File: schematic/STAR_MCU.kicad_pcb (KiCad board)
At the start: 2 copper layers, 168 parts, among them J11 6120XX21621_61200621621, J13 6120XX21621_61200821621, J14 6120XX21621_61200821621, J15 6120XX21621_61200821621, J16 6120XX21621_61200821621, J17 SSW-106-02-G-S-RA, J18 6120XX21621_61200621621, J19 6120XX21621_61200821621, J2 USB4216-03-A, J20 S5B-XH-A, J21 6120XX21621_61200621621, J22 SSW-106-02-G-S-RA, J23 Conn_02x20_Odd_Even, J24 HC-SR04, J25 HC-SR04, J26 HC-SR04, J27 HC-SR04, J28 Conn_01x02, J31 SSW-106-02-G-S-RA, J32 SSW-106-02-G-S-RA, J4 E1E2-Emulator-Interface, J5 SSW-106-02-G-S-RA, J6 SSW-106-02-G-D-RA, J7 USB4216-03-A, J8 Conn_02x20_Odd_Even, U1 R5F572NNHGFP-30, U2 CY7C65213A-28PVXI, U3 TVS2200DRV, U4 LDL1117S33R, U5 TPS2116DRLR, U6 TVS2200DRV, U7 DS18B20+

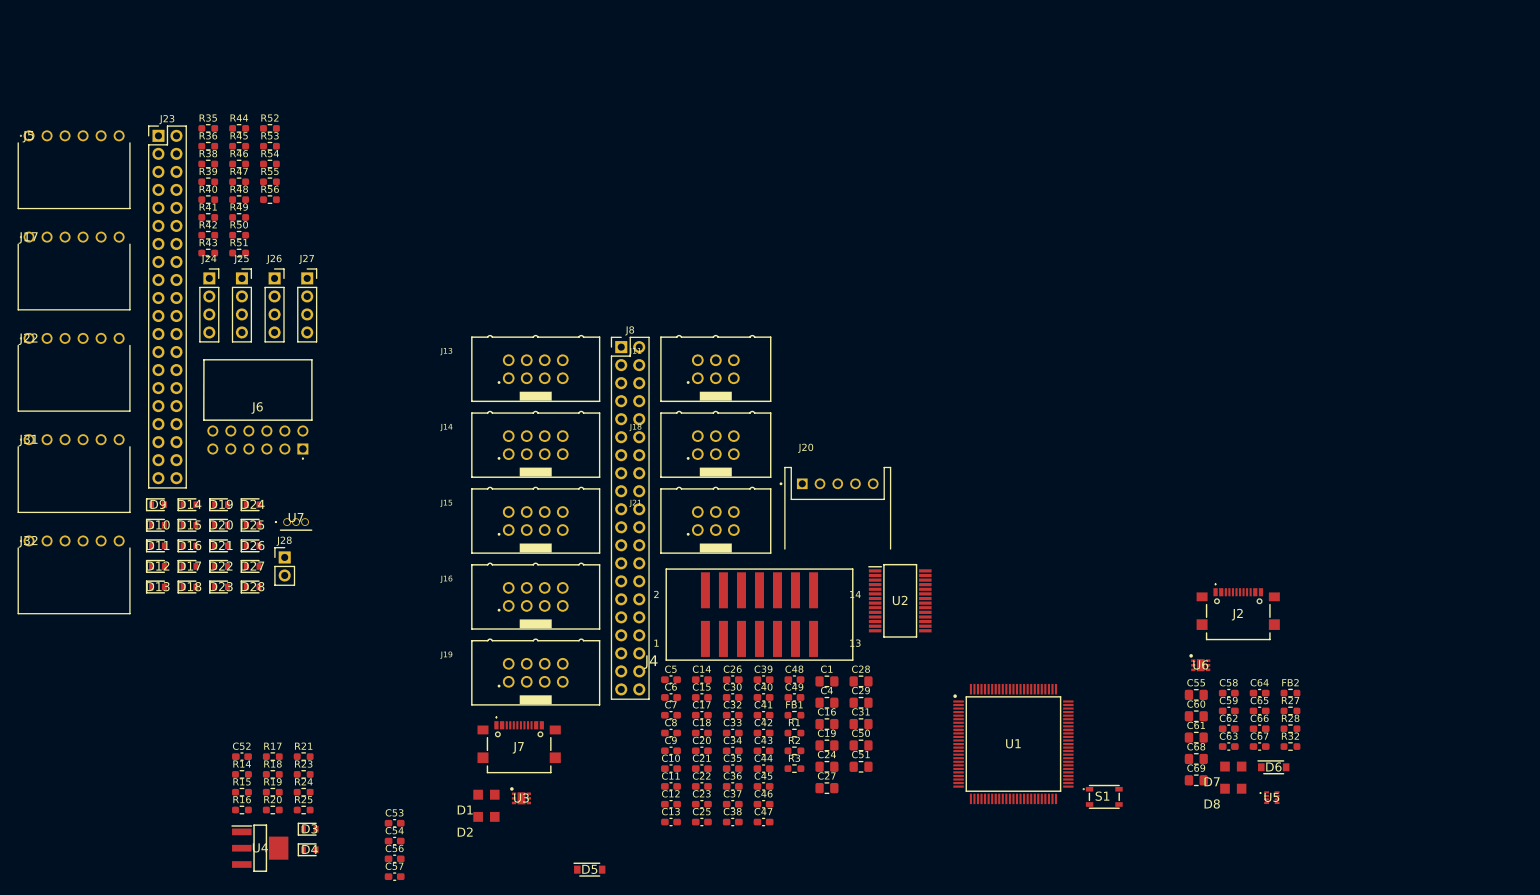
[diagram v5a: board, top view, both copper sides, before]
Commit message: docs(schematic): update KiCad file headers
Standardize schematic file metadata:
- Update date to 2026-01-01
- Update copyright to STAR Project
- Ensure consistency with firmware file headers
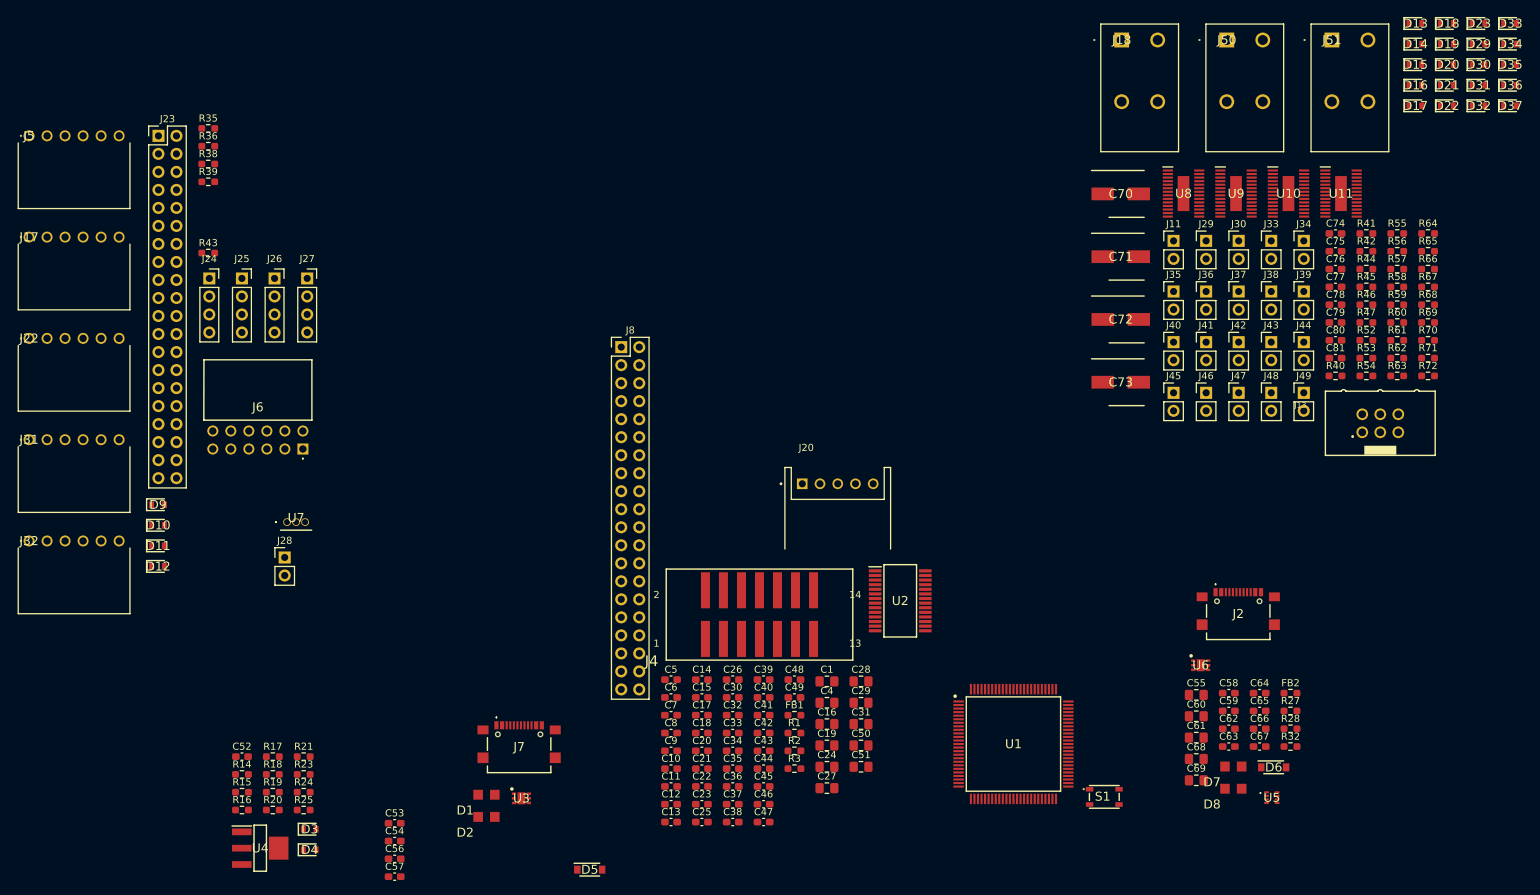
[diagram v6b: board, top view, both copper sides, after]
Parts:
- removed D24, D25, D26, D27, D28: RED, SML-D12Y1WT86:LEDC1608X55N
- removed J14, J15, J16, J19: 6120XX21621_61200821621, 61200821621:61200821621
- removed J21: 6120XX21621_61200621621, 61200621621:61200621621
- removed R48, R49, R50, R51: 68R, Resistor_SMD:R_0603_1608Metric_Pad0.98x0.95mm_HandSolder
- added C70: 56u, 865080343007:CAPAE660X550N, F.Cu at (197.9, 46.3)
- added C71: 56u, 865080343007:CAPAE660X550N, F.Cu at (197.9, 55.2)
- added C72: 56u, 865080343007:CAPAE660X550N, F.Cu at (197.9, 64.0)
- added C73: 56u, 865080343007:CAPAE660X550N, F.Cu at (197.9, 72.9)
- added C74: 220n, Capacitor_SMD:C_0603_1608Metric_Pad1.08x0.95mm_HandSolder, F.Cu at (228.1, 51.9)
- added C75: 220n, Capacitor_SMD:C_0603_1608Metric_Pad1.08x0.95mm_HandSolder, F.Cu at (228.1, 54.4)
- added C76: 220n, Capacitor_SMD:C_0603_1608Metric_Pad1.08x0.95mm_HandSolder, F.Cu at (228.1, 56.9)
- added C77: 220n, Capacitor_SMD:C_0603_1608Metric_Pad1.08x0.95mm_HandSolder, F.Cu at (228.1, 59.5)
- added C78: 100n, Capacitor_SMD:C_0603_1608Metric_Pad1.08x0.95mm_HandSolder, F.Cu at (228.1, 62.0)
- added C79: 100n, Capacitor_SMD:C_0603_1608Metric_Pad1.08x0.95mm_HandSolder, F.Cu at (228.1, 64.5)
- added C80: 100n, Capacitor_SMD:C_0603_1608Metric_Pad1.08x0.95mm_HandSolder, F.Cu at (228.1, 67.0)
- added C81: 100n, Capacitor_SMD:C_0603_1608Metric_Pad1.08x0.95mm_HandSolder, F.Cu at (228.1, 69.5)
- added D29: RED, SML-D12Y1WT86:LEDC1608X55N, F.Cu at (248.3, 25.2)
- added D30: RED, SML-D12Y1WT86:LEDC1608X55N, F.Cu at (248.3, 28.1)
- added D31: RED, SML-D12Y1WT86:LEDC1608X55N, F.Cu at (248.3, 31.0)
- added D32: RED, SML-D12Y1WT86:LEDC1608X55N, F.Cu at (248.3, 33.9)
- added D33: RED, SML-D12Y1WT86:LEDC1608X55N, F.Cu at (252.8, 22.3)
- added D34: RED, SML-D12Y1WT86:LEDC1608X55N, F.Cu at (252.8, 25.2)
- added D35: RED, SML-D12Y1WT86:LEDC1608X55N, F.Cu at (252.8, 28.1)
- added D36: RED, SML-D12Y1WT86:LEDC1608X55N, F.Cu at (252.8, 31.0)
- added D37: RED, SML-D12Y1WT86:LEDC1608X55N, F.Cu at (252.8, 33.9)
- added J29: Conn_01x02, Connector_PinHeader_2.54mm:PinHeader_1x02_P2.54mm_Vertical, F.Cu at (209.9, 53.0)
- added J30: Conn_01x02, Connector_PinHeader_2.54mm:PinHeader_1x02_P2.54mm_Vertical, F.Cu at (214.5, 53.0)
- added J33: Conn_01x02, Connector_PinHeader_2.54mm:PinHeader_1x02_P2.54mm_Vertical, F.Cu at (219.1, 53.0)
- added J34: Conn_01x02, Connector_PinHeader_2.54mm:PinHeader_1x02_P2.54mm_Vertical, F.Cu at (223.7, 53.0)
- added J35: Conn_01x02, Connector_PinHeader_2.54mm:PinHeader_1x02_P2.54mm_Vertical, F.Cu at (205.3, 60.1)
- added J36: Conn_01x02, Connector_PinHeader_2.54mm:PinHeader_1x02_P2.54mm_Vertical, F.Cu at (209.9, 60.1)
- added J37: Conn_01x02, Connector_PinHeader_2.54mm:PinHeader_1x02_P2.54mm_Vertical, F.Cu at (214.5, 60.1)
- added J38: Conn_01x02, Connector_PinHeader_2.54mm:PinHeader_1x02_P2.54mm_Vertical, F.Cu at (219.1, 60.1)
- added J39: Conn_01x02, Connector_PinHeader_2.54mm:PinHeader_1x02_P2.54mm_Vertical, F.Cu at (223.7, 60.1)
- added J40: Conn_01x02, Connector_PinHeader_2.54mm:PinHeader_1x02_P2.54mm_Vertical, F.Cu at (205.3, 67.2)
- added J41: Conn_01x02, Connector_PinHeader_2.54mm:PinHeader_1x02_P2.54mm_Vertical, F.Cu at (209.9, 67.2)
- added J42: Conn_01x02, Connector_PinHeader_2.54mm:PinHeader_1x02_P2.54mm_Vertical, F.Cu at (214.5, 67.2)
- added J43: Conn_01x02, Connector_PinHeader_2.54mm:PinHeader_1x02_P2.54mm_Vertical, F.Cu at (219.1, 67.2)
- added J44: Conn_01x02, Connector_PinHeader_2.54mm:PinHeader_1x02_P2.54mm_Vertical, F.Cu at (223.7, 67.2)
- added J45: Conn_01x02, Connector_PinHeader_2.54mm:PinHeader_1x02_P2.54mm_Vertical, F.Cu at (205.3, 74.4)
- added J46: Conn_01x02, Connector_PinHeader_2.54mm:PinHeader_1x02_P2.54mm_Vertical, F.Cu at (209.9, 74.4)
- added J47: Conn_01x02, Connector_PinHeader_2.54mm:PinHeader_1x02_P2.54mm_Vertical, F.Cu at (214.5, 74.4)
- added J48: Conn_01x02, Connector_PinHeader_2.54mm:PinHeader_1x02_P2.54mm_Vertical, F.Cu at (219.1, 74.4)
- added J49: Conn_01x02, Connector_PinHeader_2.54mm:PinHeader_1x02_P2.54mm_Vertical, F.Cu at (223.7, 74.4)
- added J50: 1017491, 1017491:1017491, F.Cu at (212.8, 24.6)
- added J51: 1017491, 1017491:1017491, F.Cu at (227.6, 24.6)
- added R57: 68R, Resistor_SMD:R_0603_1608Metric_Pad0.98x0.95mm_HandSolder, F.Cu at (236.8, 56.9)
- added R58: 68R, Resistor_SMD:R_0603_1608Metric_Pad0.98x0.95mm_HandSolder, F.Cu at (236.8, 59.5)
- added R59: 68R, Resistor_SMD:R_0603_1608Metric_Pad0.98x0.95mm_HandSolder, F.Cu at (236.8, 62.0)
- added R60: 68R, Resistor_SMD:R_0603_1608Metric_Pad0.98x0.95mm_HandSolder, F.Cu at (236.8, 64.5)
- added R61: 68R, Resistor_SMD:R_0603_1608Metric_Pad0.98x0.95mm_HandSolder, F.Cu at (236.8, 67.0)
- added R62: 68R, Resistor_SMD:R_0603_1608Metric_Pad0.98x0.95mm_HandSolder, F.Cu at (236.8, 69.5)
- added R63: 68R, Resistor_SMD:R_0603_1608Metric_Pad0.98x0.95mm_HandSolder, F.Cu at (236.8, 72.0)
- added R64: 68R, Resistor_SMD:R_0603_1608Metric_Pad0.98x0.95mm_HandSolder, F.Cu at (241.2, 51.9)
- added R65: 68R, Resistor_SMD:R_0603_1608Metric_Pad0.98x0.95mm_HandSolder, F.Cu at (241.2, 54.4)
- added R66: 68R, Resistor_SMD:R_0603_1608Metric_Pad0.98x0.95mm_HandSolder, F.Cu at (241.2, 56.9)
- added R67: 68R, Resistor_SMD:R_0603_1608Metric_Pad0.98x0.95mm_HandSolder, F.Cu at (241.2, 59.5)
- added R68: 68R, Resistor_SMD:R_0603_1608Metric_Pad0.98x0.95mm_HandSolder, F.Cu at (241.2, 62.0)
- added R69: 3k16, Resistor_SMD:R_0603_1608Metric_Pad0.98x0.95mm_HandSolder, F.Cu at (241.2, 64.5)
- added R70: 3k16, Resistor_SMD:R_0603_1608Metric_Pad0.98x0.95mm_HandSolder, F.Cu at (241.2, 67.0)
- added R71: 3k16, Resistor_SMD:R_0603_1608Metric_Pad0.98x0.95mm_HandSolder, F.Cu at (241.2, 69.5)
- added R72: 3k16, Resistor_SMD:R_0603_1608Metric_Pad0.98x0.95mm_HandSolder, F.Cu at (241.2, 72.0)
- added U10: DRV8243SQDGQRQ1 (S-Variant), DRV8243SQDGQRQ1:SOP50P490X110-29N, F.Cu at (221.5, 46.3)
- added U11: DRV8243SQDGQRQ1 (S-Variant), DRV8243SQDGQRQ1:SOP50P490X110-29N, F.Cu at (228.9, 46.3)
- added U8: DRV8243SQDGQRQ1 (S-Variant), DRV8243SQDGQRQ1:SOP50P490X110-29N, F.Cu at (206.7, 46.3)
- added U9: DRV8243SQDGQRQ1 (S-Variant), DRV8243SQDGQRQ1:SOP50P490X110-29N, F.Cu at (214.1, 46.3)
- J11: value 6120XX21621_61200621621 -> Conn_01x02; footprint 61200621621:61200621621 -> Connector_PinHeader_2.54mm:PinHeader_1x02_P2.54mm_Vertical
- J13: value 6120XX21621_61200821621 -> 6120XX21621_61200621621; footprint 61200821621:61200821621 -> 61200621621:61200621621
- J18: value 6120XX21621_61200621621 -> 1017491; footprint 61200621621:61200621621 -> 1017491:1017491
- R52, R53, R54, R55: value 68R -> 10k
- moved D13 194.3 mm to (239.4, 22.3)
- moved D23 194.3 mm to (248.3, 22.3)
- moved D18 194.3 mm to (243.9, 22.3)
- moved D14 184.6 mm to (239.4, 25.2)
- moved D15 184.6 mm to (239.4, 28.1)
- moved D16 184.6 mm to (239.4, 31.0)
- moved D17 184.6 mm to (239.4, 33.9)
- moved D19 184.6 mm to (243.9, 25.2)
- moved D20 184.6 mm to (243.9, 28.1)
- moved D21 184.6 mm to (243.9, 31.0)
- moved D22 184.6 mm to (243.9, 33.9)
- moved R41 163.3 mm to (232.5, 51.9)
- moved R42 163.3 mm to (232.5, 54.4)
- moved R40 160.9 mm to (228.1, 72.0)
- moved R44 160.2 mm to (232.5, 56.9)
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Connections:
- D20 pad 1: GND -> /MOTOR0_nFAULT
- D21 pad 1: GND -> /MOTOR1_nFAULT
- D22 pad 1: GND -> /MOTOR2_nFAULT
- D23 pad 1: GND -> /MOTOR3_nFAULT
- J11 pad 1: /P3V3_BUCK -> /PMOD_JC_INT1
- J11 pad 2: GND -> /BTP_INT
- J13 pad 1: /RSPIC_MOTOR0_nCS -> /BTP_INT
- J13 pad 2: /RSPIC_COPI -> /BMS_SMBUS_DATA
- J13 pad 3: /RSPIC_MOTOR1_nCS -> GND
- J13 pad 4: /RSPIC_SCLK -> /BMS_SMBUS_CLK
- J13 pad 5: /RSPIC_MOTOR2_nCS -> GND
- J13 pad 6: /RSPIC_CIPO -> GND
- J18 pad 2: /FUEL_GUAGE_SMBC_SCL -> GND
- J18 pad 3: /P3V3_BUCK -> /P6V0_BUCK
- J18 pad 4: /FUEL_GUAGE_SMBD_SDA -> /P6V0_BUCK
- J23 pad 10: unconnected-(J23-Pin_10-Pad10) -> /LiDAR_TX_PI5_RX
- J23 pad 11: unconnected-(J23-Pin_11-Pad11) -> /PI_PIN_11
- J23 pad 12: unconnected-(J23-Pin_12-Pad12) -> /PI_PIN_12
- J23 pad 13: unconnected-(J23-Pin_13-Pad13) -> /PI_PIN_13
- J23 pad 15: unconnected-(J23-Pin_15-Pad15) -> /PI_PIN_15
- J23 pad 16: unconnected-(J23-Pin_16-Pad16) -> /IMU_RST
- J23 pad 18: unconnected-(J23-Pin_18-Pad18) -> /IMU_INT
- J23 pad 19: unconnected-(J23-Pin_19-Pad19) -> /PI_PIN_19
- J23 pad 21: unconnected-(J23-Pin_21-Pad21) -> /PI_PIN_21
- J23 pad 22: unconnected-(J23-Pin_22-Pad22) -> /PI_PIN_22
- J23 pad 23: unconnected-(J23-Pin_23-Pad23) -> /PI_PIN_23
- J23 pad 24: unconnected-(J23-Pin_24-Pad24) -> /PI_PIN_24
- J23 pad 26: unconnected-(J23-Pin_26-Pad26) -> /PI_PIN_26
- J23 pad 27: unconnected-(J23-Pin_27-Pad27) -> /PI_PIN_27
- J23 pad 28: unconnected-(J23-Pin_28-Pad28) -> /PI_PIN_28
- J23 pad 29: unconnected-(J23-Pin_29-Pad29) -> /PI_PIN_29
- J23 pad 3: unconnected-(J23-Pin_3-Pad3) -> /PI_PIN_3
- J23 pad 31: unconnected-(J23-Pin_31-Pad31) -> /PI_PIN_31
- J23 pad 32: unconnected-(J23-Pin_32-Pad32) -> /PI_PIN_32
- J23 pad 33: unconnected-(J23-Pin_33-Pad33) -> /PI_PIN_33
- J23 pad 35: unconnected-(J23-Pin_35-Pad35) -> /PI_PIN_35
- J23 pad 36: unconnected-(J23-Pin_36-Pad36) -> /PI_PIN_36
- J23 pad 37: unconnected-(J23-Pin_37-Pad37) -> /PI_PIN_37
- J23 pad 38: unconnected-(J23-Pin_38-Pad38) -> /PI_PIN_38
- J23 pad 40: unconnected-(J23-Pin_40-Pad40) -> /PI_PIN_40
- J23 pad 5: unconnected-(J23-Pin_5-Pad5) -> /PI_PIN_5
- J23 pad 7: unconnected-(J23-Pin_7-Pad7) -> /PI_PIN_7
- J23 pad 8: unconnected-(J23-Pin_8-Pad8) -> /LiDAR_RX_PI5_TX
- J28 pad 1: unconnected-(J28-Pin_1-Pad1) -> /PMOD_JC_INT1
- J28 pad 2: unconnected-(J28-Pin_2-Pad2) -> Net-(J28-Pin_2)
- J8 pad 11: unconnected-(J8-Pin_11-Pad11) -> /PI_PIN_11
- J8 pad 12: unconnected-(J8-Pin_12-Pad12) -> /PI_PIN_12
- J8 pad 13: unconnected-(J8-Pin_13-Pad13) -> /PI_PIN_13
- J8 pad 15: unconnected-(J8-Pin_15-Pad15) -> /PI_PIN_15
- J8 pad 19: /RPI5_RSPIA_COPI -> /PI_PIN_19
- J8 pad 21: /RPI5_RSPIA_CIPO -> /PI_PIN_21
- J8 pad 22: unconnected-(J8-Pin_22-Pad22) -> /PI_PIN_22
- J8 pad 23: /RPI5_RSPIA_SCLK -> /PI_PIN_23
- J8 pad 24: /RPI5_RSPIA_CS -> /PI_PIN_24
- J8 pad 26: unconnected-(J8-Pin_26-Pad26) -> /PI_PIN_26
- J8 pad 27: unconnected-(J8-Pin_27-Pad27) -> /PI_PIN_27
- J8 pad 28: unconnected-(J8-Pin_28-Pad28) -> /PI_PIN_28
- J8 pad 29: unconnected-(J8-Pin_29-Pad29) -> /PI_PIN_29
- J8 pad 3: /PI_SDA -> /PI_PIN_3
- J8 pad 31: unconnected-(J8-Pin_31-Pad31) -> /PI_PIN_31
- J8 pad 32: unconnected-(J8-Pin_32-Pad32) -> /PI_PIN_32
- J8 pad 33: unconnected-(J8-Pin_33-Pad33) -> /PI_PIN_33
- J8 pad 35: unconnected-(J8-Pin_35-Pad35) -> /PI_PIN_35
- J8 pad 36: unconnected-(J8-Pin_36-Pad36) -> /PI_PIN_36
- J8 pad 37: unconnected-(J8-Pin_37-Pad37) -> /PI_PIN_37
- J8 pad 38: unconnected-(J8-Pin_38-Pad38) -> /PI_PIN_38
- J8 pad 40: unconnected-(J8-Pin_40-Pad40) -> /PI_PIN_40
- J8 pad 5: /PI_SCL -> /PI_PIN_5
- J8 pad 7: unconnected-(J8-Pin_7-Pad7) -> /PI_PIN_7
- R1 pad 1: /PI_SDA -> /PI_PIN_3
- R2 pad 1: /PI_SCL -> /PI_PIN_5
- R35 pad 1: /PMOD_JC_INT1 -> Net-(J28-Pin_2)
- R36 pad 1: /PMOD_JC_INT2 -> Net-(J29-Pin_2)
- R38 pad 1: /PMOD_JC_SCL -> Net-(J30-Pin_2)
- R39 pad 1: /PMOD_JC_SDA -> Net-(J33-Pin_2)
- R40 pad 1: /PMOD_JF_GPIO0 -> Net-(J38-Pin_2)
- R41 pad 1: /PMOD_JF_GPIO1 -> Net-(J44-Pin_2)
- R42 pad 1: /PMOD_JF_SCL -> Net-(J45-Pin_2)
- R44 pad 1: /PMOD_JF_SDA -> Net-(J46-Pin_2)
- R45 pad 1: /PMOD_JD_GPIO0 -> Net-(J47-Pin_2)
- R46 pad 1: /PMOD_JD_GPIO1 -> Net-(J48-Pin_2)
- R47 pad 1: /PMOD_JD_GPIO2 -> Net-(J49-Pin_2)
- R52 pad 1: /PMOD_JA_CS0 -> /MOTOR0_nFAULT
- R52 pad 2: Net-(D24-Pad2) -> /P3V3_BUCK
- R53 pad 1: /PMOD_JA_CS1 -> /MOTOR2_nFAULT
- R53 pad 2: Net-(D25-Pad2) -> /P3V3_BUCK
- R54 pad 1: /PMOD_JA_GPIO -> /MOTOR1_nFAULT
- R54 pad 2: Net-(D26-Pad2) -> /P3V3_BUCK
- R55 pad 1: /PMOD_JA_RST -> /MOTOR3_nFAULT
- R55 pad 2: Net-(D27-Pad2) -> /P3V3_BUCK
- R56 pad 1: /PMOD_JA_DC -> /P3V3_BUCK
- R56 pad 2: Net-(D28-Pad2) -> Net-(D20-Pad2)
- U1 pad 100: /PMOD_JF_GPIO0 -> /DS18B20_DQ
- U1 pad 23: /ENCODER2_PHASE_A -> /ENCODER3_PHASE_A
- U1 pad 26: /ENCODER0_PHASE_B -> /ENCODER1_PHASE_B
- U1 pad 32: /ENCODER0_PHASE_A -> /ENCODER1_PHASE_A
- U1 pad 4: /PMOD_JE_GPIO3 -> /PMOD_JE_GPIO0
- U1 pad 51: /ENCODER1_PHASE_A -> /ENCODER2_PHASE_A
- U1 pad 52: /ENCODER1_PHASE_B -> /ENCODER2_PHASE_B
- U1 pad 59: /PMOD_JE_GPIO2 -> /PMOD_JE_GPIO1
- U1 pad 61: /DS18B20_DQ -> /PMOD_JE_GPIO2
- U1 pad 63: /RPI5_RSPIA_CIPO -> /PI_PIN_21
- U1 pad 64: /RPI5_RSPIA_COPI -> /PI_PIN_19
- U1 pad 65: /RPI5_RSPIA_SCLK -> /PI_PIN_23
- U1 pad 66: /RPI5_RSPIA_CS -> /PI_PIN_24
- U1 pad 67: /ENCODER2_PHASE_B -> /ENCODER3_PHASE_B
- U1 pad 69: /PMOD_JF_GPIO1 -> /PMOD_JE_GPIO3
- U1 pad 71: /MOTOR2_PH -> /MOTOR3_PH
- U1 pad 72: /MOTOR2_EN -> /MOTOR3_EN
- U1 pad 74: /MOTOR0_PH -> /MOTOR1_PH
- U1 pad 75: /MOTOR1_PH -> /MOTOR2_PH
- U1 pad 77: /MOTOR0_EN -> /MOTOR1_EN
- U1 pad 78: /MOTOR1_EN -> /MOTOR2_EN
- U1 pad 86: /PMOD_JE_GPIO1 -> /PMOD_JF_GPIO0
- U1 pad 87: /MOTOR2_nFAULT -> /MOTOR3_nFAULT
- U1 pad 88: /MOTOR1_nFAULT -> /MOTOR2_nFAULT
- U1 pad 89: /MOTOR0_nFAULT -> /MOTOR1_nFAULT
- U1 pad 91: /MOTOR2_IPROPI -> /MOTOR3_IPROPI
- U1 pad 92: /MOTOR1_IPROPI -> /MOTOR2_IPROPI
- U1 pad 93: /MOTOR0_IPROPI -> /MOTOR1_IPROPI
- U1 pad 98: /PMOD_JE_GPIO0 -> /PMOD_JF_GPIO1
- U2 pad 1: /SCI9_RXD1 -> /SCI9_RXD9
